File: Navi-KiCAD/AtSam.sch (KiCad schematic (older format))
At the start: 42 parts, among them U4 ATSAME70Q21A-AN, Y1 9HT11-32.768KDZB-T, Y2 7V-16.000MAHJ-T

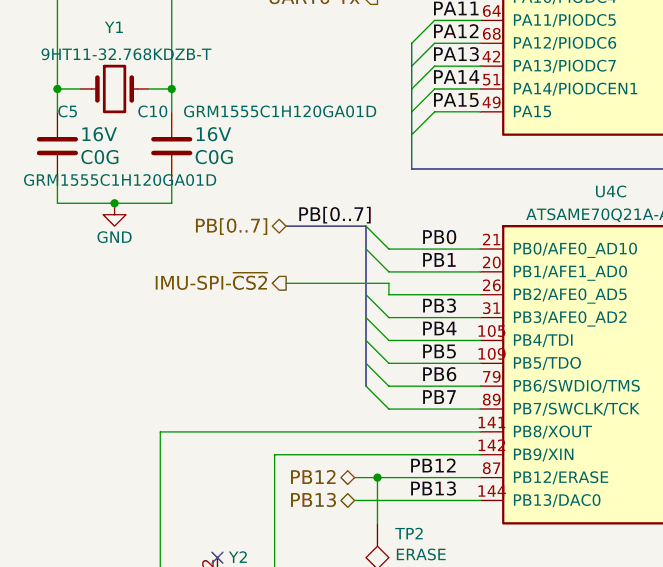
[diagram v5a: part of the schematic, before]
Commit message: Tweaked pinouts and finished routing known connectors. Now for the remaining IO.
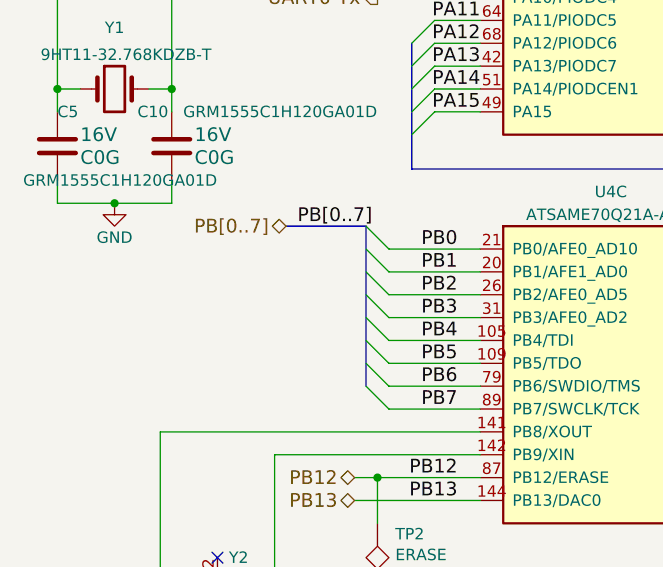
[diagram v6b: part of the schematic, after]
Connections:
- net IMU-SPI-~CS2 renamed PB2
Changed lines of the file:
@@
 $EndComp
 $Comp
-L +3.3V #PWR150
+L +3.3V #PWR0145
 U 1 1 58B891F6
 P 6200 900
-F 0 "#PWR150" H 4500 -1600 50  0001 C CNN
+F 0 "#PWR0145" H 4500 -1600 50  0001 C CNN
 F 1 "+3.3V" H 6215 1073 50  0000 C CNN
 F 2 "" H 4500 -1450 50  0001 C CNN
@@
 $EndComp
 $Comp
-L GND #PWR141
+L GND #PWR0146
 U 1 1 58B89232
 P 2400 2800
-F 0 "#PWR141" H 1100 750 50  0001 C CNN
+F 0 "#PWR0146" H 1100 750 50  0001 C CNN
 F 1 "GND" H 2405 2627 50  0000 C CNN
 F 2 "" H 1100 1000 50  0001 C CNN
@@
 $EndComp
 $Comp
-L GND #PWR142
+L GND #PWR0147
 U 1 1 58B892B4
 P 4300 2800
-F 0 "#PWR142" H 3000 750 50  0001 C CNN
+F 0 "#PWR0147" H 3000 750 50  0001 C CNN
 F 1 "GND" H 4305 2627 50  0000 C CNN
 F 2 "" H 3000 1000 50  0001 C CNN
@@
 $EndComp
 $Comp
-L GND #PWR153
+L GND #PWR0148
 U 1 1 58B8B12B
 P 10250 6200
-F 0 "#PWR153" H 8950 4150 50  0001 C CNN
+F 0 "#PWR0148" H 8950 4150 50  0001 C CNN
 F 1 "GND" H 10255 6027 50  0000 C CNN
 F 2 "" H 8950 4400 50  0001 C CNN
@@
 VBUS_DETECT
 $Comp
-L VUSB #PWR157
+L VUSB #PWR0149
 U 1 1 58B8B57E
 P 10850 5700
-F 0 "#PWR157" H 10900 5750 50  0001 C CNN
+F 0 "#PWR0149" H 10900 5750 50  0001 C CNN
 F 1 "VUSB" H 10865 5873 50  0000 C CNN
 F 2 "" H 150 450 50  0001 C CNN
@@
 	650  5200 650  5100
 $Comp
-L GND #PWR128
+L GND #PWR0150
 U 1 1 58B9AEC4
 P 900 5200
-F 0 "#PWR128" H 900 4950 50  0001 C CNN
+F 0 "#PWR0150" H 900 4950 50  0001 C CNN
 F 1 "GND" H 900 5050 50  0000 C CNN
 F 2 "" H 900 5200 50  0001 C CNN
@@
 	1100 7600 1100 7500
 $Comp
-L GND #PWR131
+L GND #PWR0151
 U 1 1 58BA68B9
 P 1350 7600
-F 0 "#PWR131" H 1350 7350 50  0001 C CNN
+F 0 "#PWR0151" H 1350 7350 50  0001 C CNN
 F 1 "GND" H 1350 7450 50  0000 C CNN
 F 2 "" H 1350 7600 50  0001 C CNN
@@
 Connection ~ 5800 1000
 $Comp
-L GND #PWR149
+L GND #PWR0152
 U 1 1 58B7BFAA
 P 5800 1300
-F 0 "#PWR149" H 4500 -750 50  0001 C CNN
+F 0 "#PWR0152" H 4500 -750 50  0001 C CNN
 F 1 "GND" H 5805 1127 50  0000 C CNN
 F 2 "" H 4500 -500 50  0001 C CNN
@@
 $EndComp
 $Comp
-L GND #PWR151
+L GND #PWR0153
 U 1 1 58B7C131
 P 6200 1300
-F 0 "#PWR151" H 4900 -750 50  0001 C CNN
+F 0 "#PWR0153" H 4900 -750 50  0001 C CNN
 F 1 "GND" H 6205 1127 50  0000 C CNN
 F 2 "" H 4900 -500 50  0001 C CNN
@@
 $EndComp
 $Comp
-L GND #PWR147
+L GND #PWR0154
 U 1 1 58B7D83B
 P 5300 1400
-F 0 "#PWR147" H 4000 -650 50  0001 C CNN
+F 0 "#PWR0154" H 4000 -650 50  0001 C CNN
 F 1 "GND" H 5300 1300 50  0000 C CNN
 F 2 "" H 4000 -400 50  0001 C CNN
@@
 $EndComp
 $Comp
-L GND #PWR146
+L GND #PWR0155
 U 1 1 58B7D876
 P 5100 1400
-F 0 "#PWR146" H 3800 -650 50  0001 C CNN
+F 0 "#PWR0155" H 3800 -650 50  0001 C CNN
 F 1 "GND" H 5100 1300 50  0000 C CNN
 F 2 "" H 3800 -400 50  0001 C CNN
@@
 $EndComp
 $Comp
-L GND #PWR145
+L GND #PWR0156
 U 1 1 58B7D8B1
 P 4900 1400
-F 0 "#PWR145" H 3600 -650 50  0001 C CNN
+F 0 "#PWR0156" H 3600 -650 50  0001 C CNN
 F 1 "GND" H 4900 1300 50  0000 C CNN
 F 2 "" H 3600 -400 50  0001 C CNN
@@
 $EndComp
 $Comp
-L GND #PWR144
+L GND #PWR0157
 U 1 1 58B7D8EC
 P 4700 1400
-F 0 "#PWR144" H 3400 -650 50  0001 C CNN
+F 0 "#PWR0157" H 3400 -650 50  0001 C CNN
 F 1 "GND" H 4700 1300 50  0000 C CNN
 F 2 "" H 3400 -400 50  0001 C CNN
@@
 $EndComp
 $Comp
-L GND #PWR143
+L GND #PWR0158
 U 1 1 58B7D927
 P 4500 1400
-F 0 "#PWR143" H 3200 -650 50  0001 C CNN
+F 0 "#PWR0158" H 3200 -650 50  0001 C CNN
 F 1 "GND" H 4500 1300 50  0000 C CNN
 F 2 "" H 3200 -400 50  0001 C CNN
@@
 Connection ~ 1400 1600
 $Comp
-L GND #PWR130
+L GND #PWR0159
 U 1 1 58B82BC8
 P 1150 2100
-F 0 "#PWR130" H -150 50  50  0001 C CNN
+F 0 "#PWR0159" H -150 50  50  0001 C CNN
 F 1 "GND" H 1155 1927 50  0000 C CNN
 F 2 "" H -150 300 50  0001 C CNN
@@
 $EndComp
 $Comp
-L GND #PWR132
+L GND #PWR0160
 U 1 1 58B82D5B
 P 1400 2100
-F 0 "#PWR132" H 100 50  50  0001 C CNN
+F 0 "#PWR0160" H 100 50  50  0001 C CNN
 F 1 "GND" H 1405 1927 50  0000 C CNN
 F 2 "" H 100 300 50  0001 C CNN
@@
 $EndComp
 $Comp
-L GND #PWR140
+L GND #PWR0161
 U 1 1 58B8358A
 P 2300 1400
-F 0 "#PWR140" H 1000 -650 50  0001 C CNN
+F 0 "#PWR0161" H 1000 -650 50  0001 C CNN
 F 1 "GND" H 2300 1300 50  0000 C CNN
 F 2 "" H 1000 -400 50  0001 C CNN
@@
 $EndComp
 $Comp
-L GND #PWR138
+L GND #PWR0162
 U 1 1 58B83590
 P 2100 1400
-F 0 "#PWR138" H 800 -650 50  0001 C CNN
+F 0 "#PWR0162" H 800 -650 50  0001 C CNN
 F 1 "GND" H 2100 1300 50  0000 C CNN
 F 2 "" H 800 -400 50  0001 C CNN
@@
 $EndComp
 $Comp
-L GND #PWR137
+L GND #PWR0163
 U 1 1 58B83596
 P 1900 1400
-F 0 "#PWR137" H 600 -650 50  0001 C CNN
+F 0 "#PWR0163" H 600 -650 50  0001 C CNN
 F 1 "GND" H 1900 1300 50  0000 C CNN
 F 2 "" H 600 -400 50  0001 C CNN
@@
 $EndComp
 $Comp
-L GND #PWR136
+L GND #PWR0164
 U 1 1 58B8359C
 P 1700 1400
-F 0 "#PWR136" H 400 -650 50  0001 C CNN
+F 0 "#PWR0164" H 400 -650 50  0001 C CNN
 F 1 "GND" H 1700 1300 50  0000 C CNN
 F 2 "" H 400 -400 50  0001 C CNN
@@
 $EndComp
 $Comp
-L GND #PWR133
+L GND #PWR0165
 U 1 1 58B835A2
 P 1500 1400
-F 0 "#PWR133" H 200 -650 50  0001 C CNN
+F 0 "#PWR0165" H 200 -650 50  0001 C CNN
 F 1 "GND" H 1500 1300 50  0000 C CNN
 F 2 "" H 200 -400 50  0001 C CNN
@@
 $EndComp
 $Comp
-L GND #PWR129
+L GND #PWR0166
 U 1 1 58B86F94
 P 1150 1300
-F 0 "#PWR129" H -150 -750 50  0001 C CNN
+F 0 "#PWR0166" H -150 -750 50  0001 C CNN
 F 1 "GND" H 1150 1200 50  0000 C CNN
 F 2 "" H -150 -500 50  0001 C CNN
@@
 $EndComp
 $Comp
-L GND #PWR127
+L GND #PWR0167
 U 1 1 58B86FE5
 P 850 1300
-F 0 "#PWR127" H -450 -750 50  0001 C CNN
+F 0 "#PWR0167" H -450 -750 50  0001 C CNN
 F 1 "GND" H 850 1200 50  0000 C CNN
 F 2 "" H -450 -500 50  0001 C CNN
@@
 $EndComp
 $Comp
-L GND #PWR148
+L GND #PWR0168
 U 1 1 58B8A103
 P 5300 1900
-F 0 "#PWR148" H 4000 -150 50  0001 C CNN
+F 0 "#PWR0168" H 4000 -150 50  0001 C CNN
 F 1 "GND" H 5305 1727 50  0000 C CNN
 F 2 "" H 4000 100 50  0001 C CNN
@@
 VDDPLLUSB
 $Comp
-L +3.3V #PWR156
+L +3.3V #PWR0169
 U 1 1 58B8D10C
 P 10850 4850
-F 0 "#PWR156" H 9150 2350 50  0001 C CNN
+F 0 "#PWR0169" H 9150 2350 50  0001 C CNN
 F 1 "+3.3V" H 10865 5023 50  0000 C CNN
 F 2 "" H 9150 2500 50  0001 C CNN
@@
 	9500 4950 10050 4950
 $Comp
-L GND #PWR152
+L GND #PWR0170
 U 1 1 58B8E11D
 P 9750 5350
-F 0 "#PWR152" H 8450 3300 50  0001 C CNN
+F 0 "#PWR0170" H 8450 3300 50  0001 C CNN
 F 1 "GND" H 9755 5177 50  0000 C CNN
 F 2 "" H 8450 3550 50  0001 C CNN
@@
 	1750 2200 1600 2200
 $Comp
-L +3.3V #PWR134
+L +3.3V #PWR0171
 U 1 1 58B9C26A
 P 1600 1900
-F 0 "#PWR134" H -100 -600 50  0001 C CNN
+F 0 "#PWR0171" H -100 -600 50  0001 C CNN
 F 1 "+3.3V" H 1600 2050 50  0000 C CNN
 F 2 "" H -100 -450 50  0001 C CNN
@@
 $EndComp
 $Comp
-L GND #PWR135
+L GND #PWR0172
 U 1 1 58B9C685
 P 1600 2200
-F 0 "#PWR135" H 300 150 50  0001 C CNN
+F 0 "#PWR0172" H 300 150 50  0001 C CNN
 F 1 "GND" H 1605 2027 50  0000 C CNN
 F 2 "" H 300 400 50  0001 C CNN
@@
 $EndComp
 $Comp
-L GND #PWR139
+L GND #PWR0173
 U 1 1 58C25D91
 P 2150 2800
-F 0 "#PWR139" H 2200 2850 50  0001 C CNN
+F 0 "#PWR0173" H 2200 2850 50  0001 C CNN
 F 1 "GND" H 2155 2627 50  0000 C CNN
 F 2 "" H -4650 -950 50  0001 C CNN
@@
 VBATT
 $Comp
-L +BATT #PWR154
+L +BATT #PWR0174
 U 1 1 58DCF8B0
 P 10850 3600
-F 0 "#PWR154" H 9800 700 50  0001 C CNN
+F 0 "#PWR0174" H 9800 700 50  0001 C CNN
 F 1 "+BATT" H 10865 3773 50  0000 C CNN
 F 2 "" H 9800 850 50  0001 C CNN
@@
 $EndComp
 $Comp
-L GND #PWR155
+L GND #PWR0175
 U 1 1 58DCFAFF
 P 10850 4300
-F 0 "#PWR155" H 9550 2250 50  0001 C CNN
+F 0 "#PWR0175" H 9550 2250 50  0001 C CNN
 F 1 "GND" H 10855 4127 50  0000 C CNN
 F 2 "" H 9550 2500 50  0001 C CNN
@@
 	10600 4300 10850 4300
 $Comp
-L PWR_FLAG #FLG19
+L PWR_FLAG #FLG0176
 U 1 1 58BDE6E5
 P 1850 1700
-F 0 "#FLG19" H -3950 -525 50  0001 C CNN
+F 0 "#FLG0176" H -3950 -525 50  0001 C CNN
 F 1 "PWR_FLAG" H 1850 1873 50  0000 C CNN
 F 2 "" H -3950 -600 50  0001 C CNN
@@
 $EndComp
 $Comp
-L PWR_FLAG #FLG20
+L PWR_FLAG #FLG0177
 U 1 1 58BDE982
 P 2150 1600
-F 0 "#FLG20" H -3650 -625 50  0001 C CNN
+F 0 "#FLG0177" H -3650 -625 50  0001 C CNN
 F 1 "PWR_FLAG" H 2150 1773 50  0000 C CNN
 F 2 "" H -3650 -700 50  0001 C CNN
@@
 Connection ~ 2150 1600
 $Comp
-L PWR_FLAG #FLG21
+L PWR_FLAG #FLG0178
 U 1 1 58BDFB15
 P 4300 2200
-F 0 "#FLG21" H -1500 -25 50  0001 C CNN
+F 0 "#FLG0178" H -1500 -25 50  0001 C CNN
 F 1 "PWR_FLAG" H 4300 2373 50  0000 C CNN
 F 2 "" H -1500 -100 50  0001 C CNN
@@
 Connection ~ 4300 2200
 $Comp
-L PWR_FLAG #FLG22
+L PWR_FLAG #FLG0179
 U 1 1 58BE124C
 P 9500 4950
-F 0 "#FLG22" H 3700 2725 50  0001 C CNN
+F 0 "#FLG0179" H 3700 2725 50  0001 C CNN
 F 1 "PWR_FLAG" V 9500 5078 50  0000 L CNN
 F 2 "" H 3700 2650 50  0001 C CNN
@@
 Text HLabel 9150 4200 2    60   Output ~ 0
 IMU-SPI-~CS1
-Text HLabel 1650 5550 0    60   Output ~ 0
-IMU-SPI-~CS2
 Wire Wire Line
 	8700 4200 9150 4200
-Wire Wire Line
-	1650 5550 2100 5550
-Wire Wire Line
-	2100 5550 2100 5600
 Text HLabel 6750 4100 0    60   Input ~ 0
 IMU-INT1
@@
 Wire Wire Line
 	7000 4100 6750 4100
+Text Label 2400 5600 2    60   ~ 0
+PB2
+Entry Wire Line
+	2000 5500 2100 5600
 $EndSCHEMATC
